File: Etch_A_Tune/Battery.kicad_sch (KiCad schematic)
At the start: 3 parts, among them IC1 BQ25170DSGR, U1 1042P, U2 BQ297xy

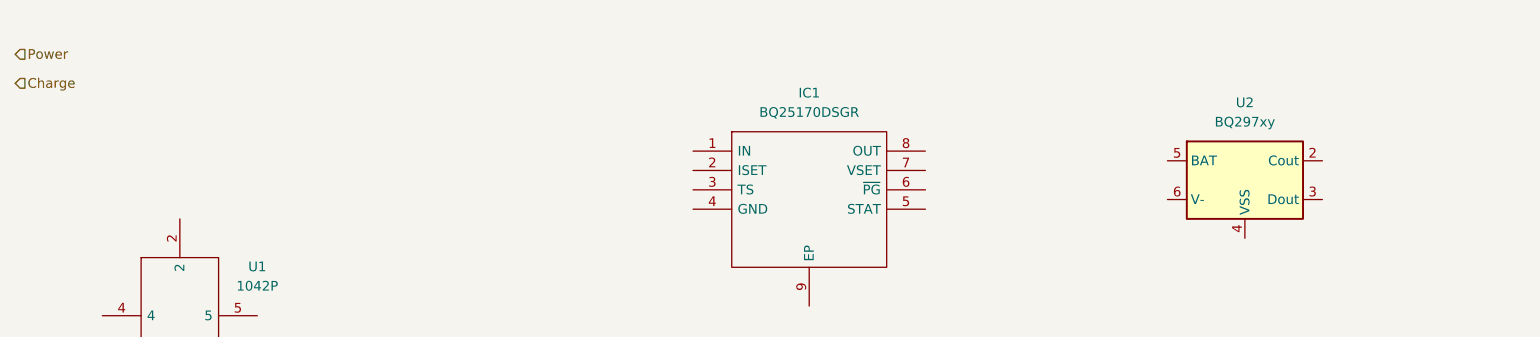
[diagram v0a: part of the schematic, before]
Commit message: Updated schematic and preliminary PCB doc
did rough PCB layout
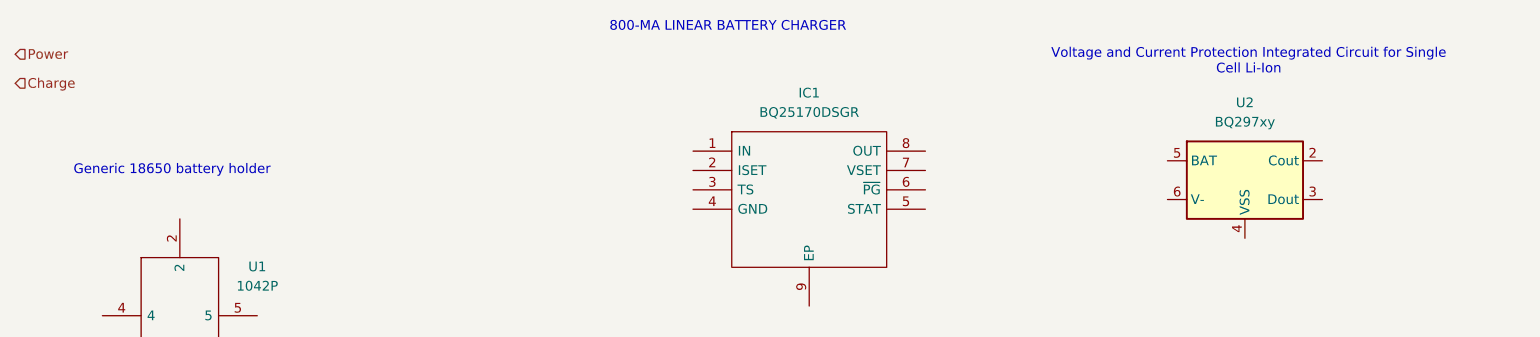
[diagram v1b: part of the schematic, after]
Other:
- note added: "800-MA LINEAR BATTERY CHARGER"
- note added: "Generic 18650 battery holder"
- note added: "Voltage and Current Protection Integrated Circuit for Single Cell Li-Ion"
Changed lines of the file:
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@@
 	(generator_version "9.0")
 	(paper "A4")
+	(text "800-MA LINEAR BATTERY CHARGER \n"
+		(exclude_from_sim no)
+		(at 140.462 45.974 0)
+		(effects
+			(font
+				(size 1.27 1.27)
+			)
+		)
+	)
+	(text "Generic 18650 battery holder\n"
+		(exclude_from_sim no)
+		(at 67.564 64.77 0)
+		(effects
+			(font
+				(size 1.27 1.27)
+			)
+		)
+	)
+	(text "Voltage and Current Protection Integrated Circuit for Single\nCell Li-Ion"
+		(exclude_from_sim no)
+		(at 208.788 50.546 0)
+		(effects
+			(font
+				(size 1.27 1.27)
+			)
+		)
+	)
 	(hierarchical_label "Charge"
 		(shape input)

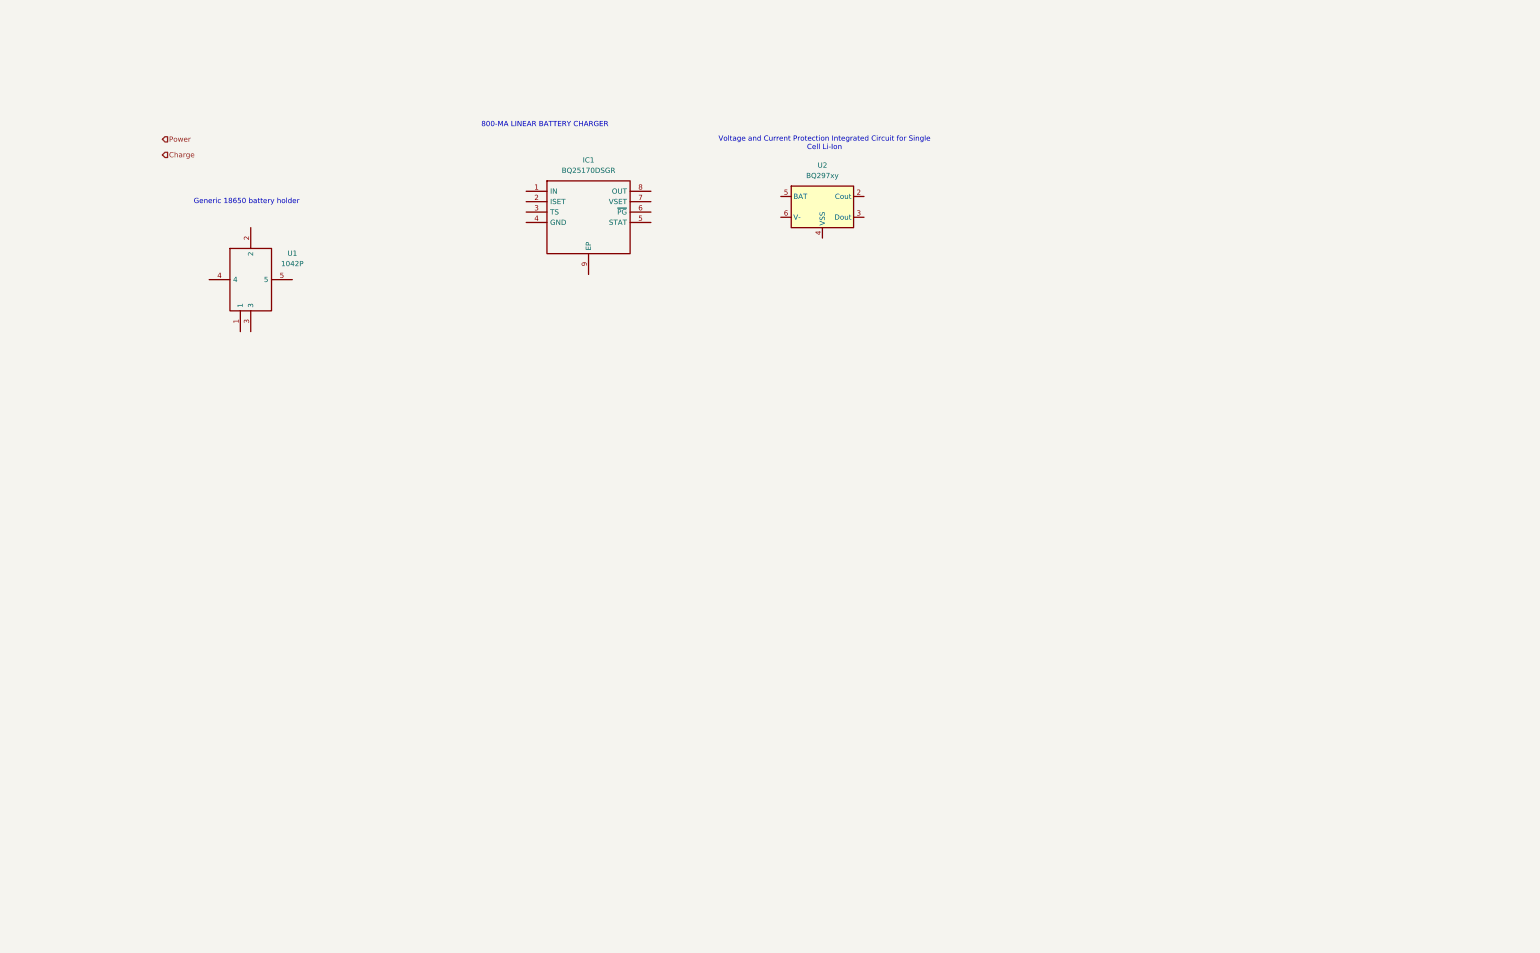
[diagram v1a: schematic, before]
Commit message: Schematic Update
Fixed component Footprints and added new switches/rotary encoders. Wired and placed bypass capacitors for most devices. Removed 5V boost converter because external DAC is no longer being utilized. Placed uC onto board design and implemented charging through USB-C connector.
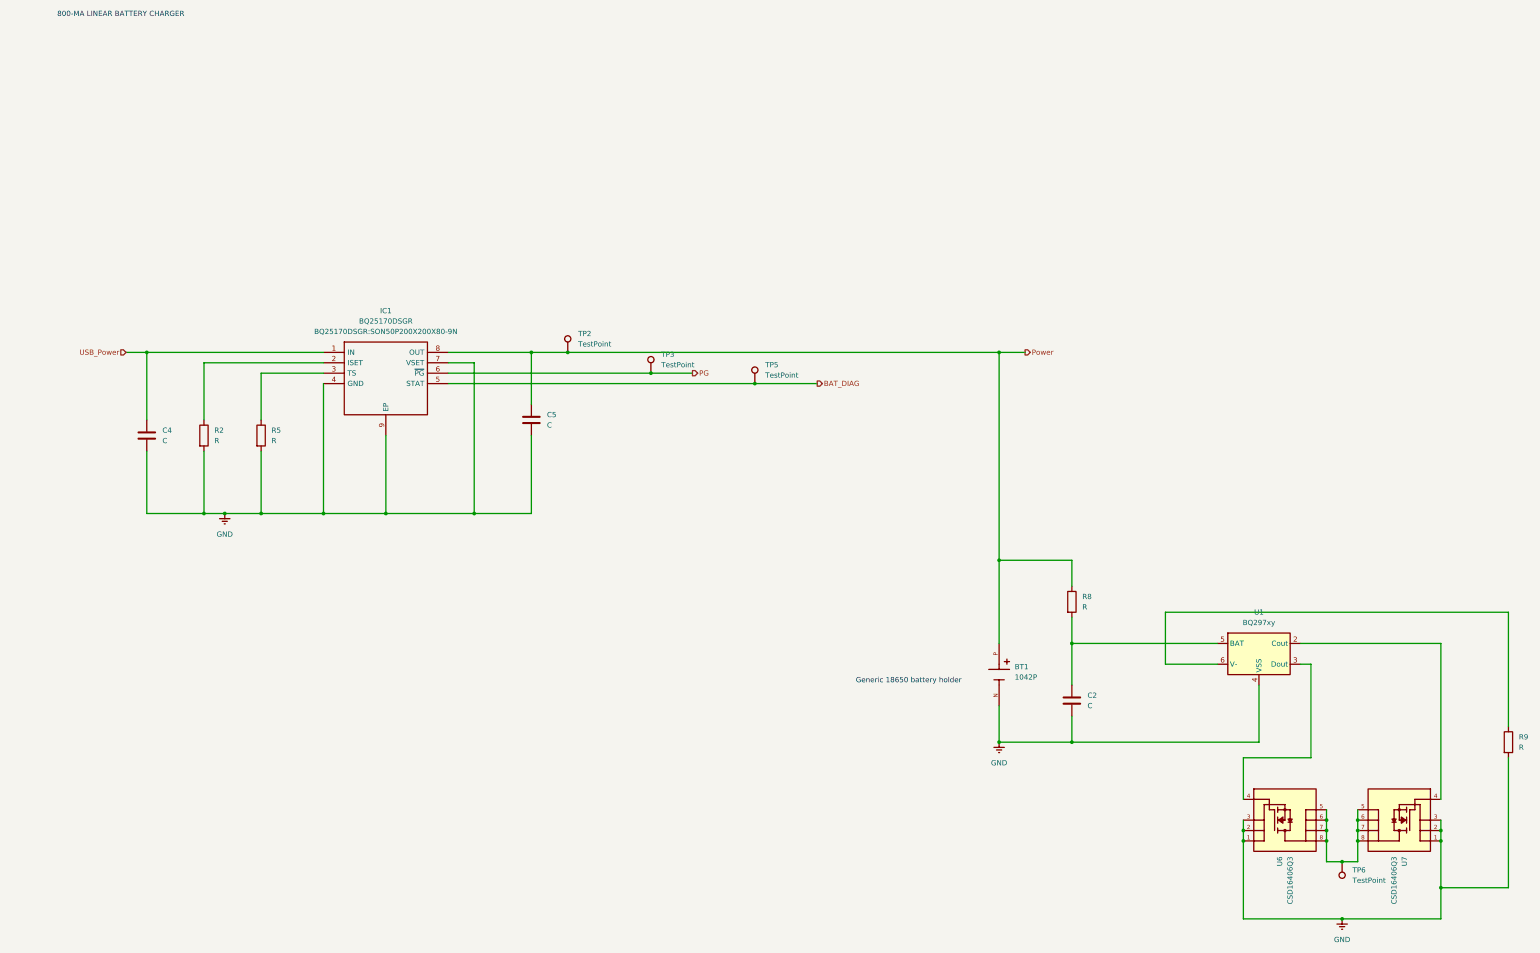
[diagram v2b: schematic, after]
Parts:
- removed U1: 1042P, 1042P, symbol SamacSys_Parts:1042P
- added BT1: 1042P, BQ25170DSGR:BAT_1042P, symbol 1042P:1042P
- added C2, C4, C5: C, symbol Device:C
- added R2, R5, R8, R9: R, symbol Device:R
- added TP2, TP3, TP5, TP6: TestPoint, TestPoint:TestPoint_Pad_D1.0mm, symbol Connector:TestPoint
- added U6, U7: CSD16406Q3, BQ25170DSGR:TRANS_CSD16406Q3, symbol CSD16406Q3:CSD16406Q3
- IC1: footprint SON50P200X200X80-9N -> BQ25170DSGR:SON50P200X200X80-9N
- renumbered U2 to U1
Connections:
- net Power: now also IC1.8 (OUT), BT1.P, C5.1, R8.1, TP2.1
- net USB_Power: now reaches IC1.1 (IN)
- net USB_Power: now also C4.1
- net at IC1.2 (ISET): now also R2.1
- net at IC1.3 (TS): now also R5.1
- net GND: now reaches IC1.4 (GND)
- net GND: now also IC1.7 (VSET), IC1.9 (EP), U1.4 (VSS), BT1.N, C2.2, C4.2, C5.2, R2.2, R5.2, R9.2, U6.1, U6.2, U6.3, U7.1, U7.2, U7.3
- net BAT_DIAG: now reaches IC1.5 (STAT)
- net BAT_DIAG: now also TP5.1
- net PG: now reaches IC1.6 (~{PG})
- net PG: now also TP3.1
- net at U1.2 (Cout): now also U7.4
- net at U1.3 (Dout): now also U6.4
- net at U1.5 (BAT): now also C2.1, R8.2
- net at U1.6 (V-): now also R9.1
- new net: TP6.1, U6.5, U6.6, U6.7, U6.8, U7.5, U7.6, U7.7, U7.8
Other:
- note removed: "Voltage and Current Protection Integrated Circuit for Single Cell Li-Ion"
- title: (none) -> Voltage and Current Protection Integrated Circuit for Single
- moved on the sheet: U1

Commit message: Etch A Tune V.02
Updated more foot prints and components onto bom, specifically SWD debug header and 1x14 pin header for touch and screen module. Added 4pin header for SD card reader.
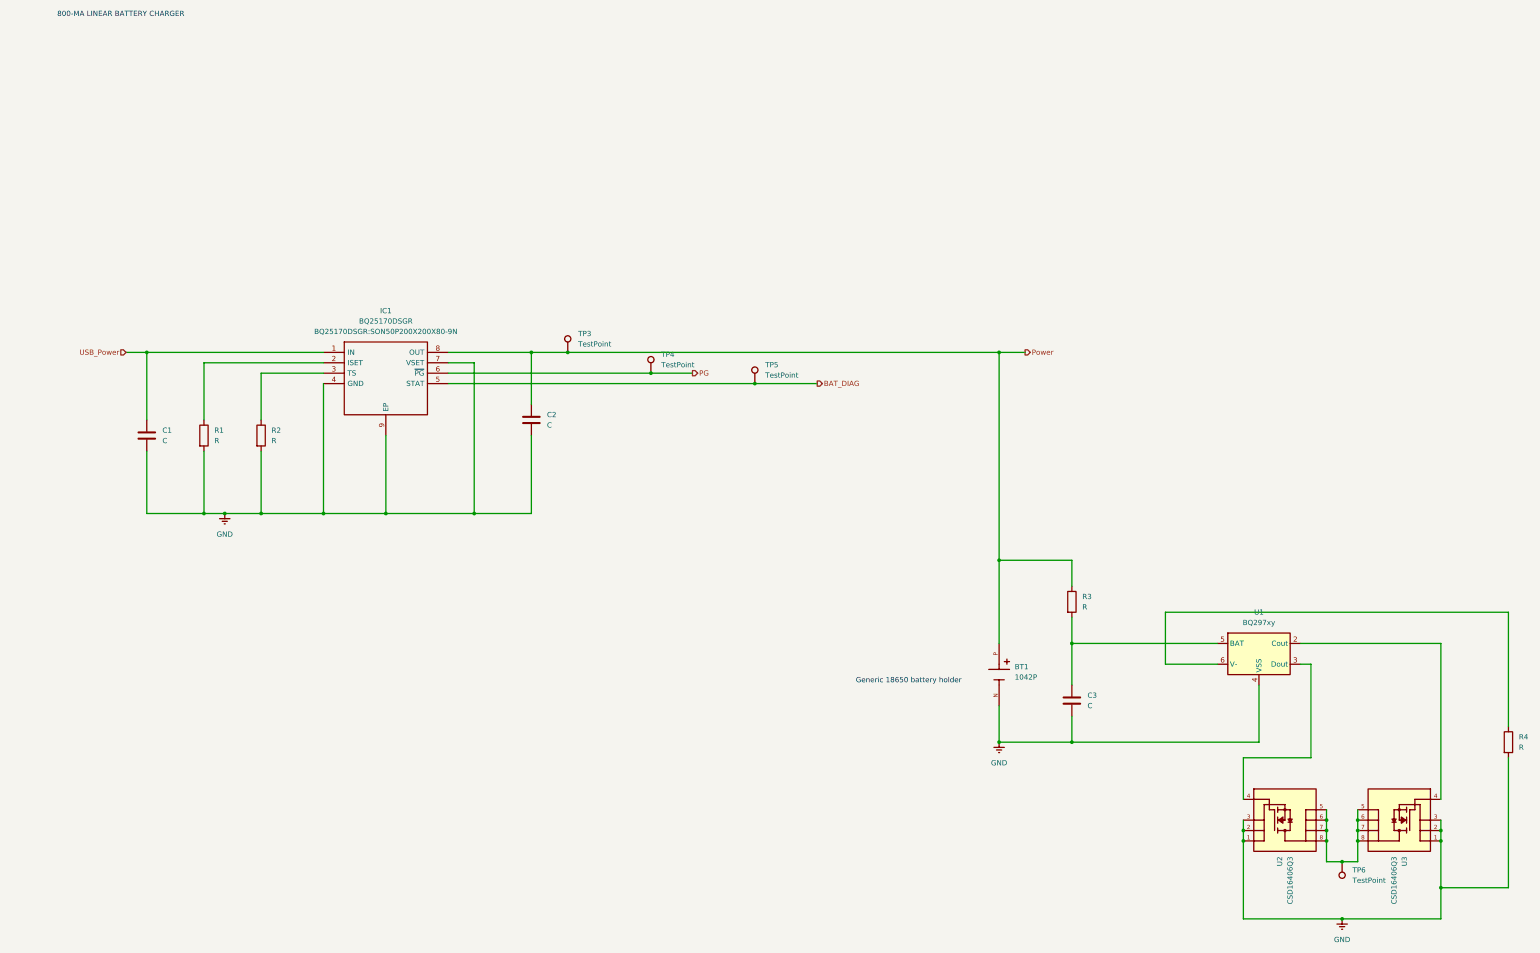
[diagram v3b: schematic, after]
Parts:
- renumbered C4 to C1, C5 to C2, C2 to C3, R2 to R1, R5 to R2, R8 to R3, R9 to R4, TP2 to TP3, TP3 to TP4, U6 to U2, U7 to U3
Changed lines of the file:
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@@
 		(on_board yes)
 		(dnp no)
-		(property "Reference" "U6"
+		(property "Reference" "U2"
 			(at 320.0399 224.79 90)
 			(effects
@@
 			(project ""
 				(path "/b4cdadf2-c4fe-48fe-ba6a-e15d1cad03b2/dd28cf9e-f503-4fc4-9cf8-d81b8295f9d5"
-					(reference "U6")
+					(reference "U2")
 					(unit 1)
 				)
@@
 		(dnp no)
 		(fields_autoplaced yes)
-		(property "Reference" "#PWR012"
+		(property "Reference" "#PWR05"
 			(at 62.23 147.32 0)
 			(effects
@@
 			(project "Etch_A_Tune"
 				(path "/b4cdadf2-c4fe-48fe-ba6a-e15d1cad03b2/dd28cf9e-f503-4fc4-9cf8-d81b8295f9d5"
-					(reference "#PWR012")
+					(reference "#PWR05")
 					(unit 1)
 				)
@@
 		(on_board yes)
 		(dnp no)
-		(property "Reference" "U7"
+		(property "Reference" "U3"
 			(at 350.5201 224.79 90)
 			(effects
@@
 			(project "Etch_A_Tune"
 				(path "/b4cdadf2-c4fe-48fe-ba6a-e15d1cad03b2/dd28cf9e-f503-4fc4-9cf8-d81b8295f9d5"
-					(reference "U7")
+					(reference "U3")
 					(unit 1)
 				)
@@
 		(dnp no)
 		(fields_autoplaced yes)
-		(property "Reference" "C2"
+		(property "Reference" "C3"
 			(at 273.05 185.4199 0)
 			(effects
@@
 			(project "Etch_A_Tune"
 				(path "/b4cdadf2-c4fe-48fe-ba6a-e15d1cad03b2/dd28cf9e-f503-4fc4-9cf8-d81b8295f9d5"
-					(reference "C2")
+					(reference "C3")
 					(unit 1)
 				)
@@
 		(dnp no)
 		(fields_autoplaced yes)
-		(property "Reference" "R2"
+		(property "Reference" "R1"
 			(at 59.69 120.6499 0)
 			(effects
@@
 			(project "Etch_A_Tune"
 				(path "/b4cdadf2-c4fe-48fe-ba6a-e15d1cad03b2/dd28cf9e-f503-4fc4-9cf8-d81b8295f9d5"
-					(reference "R2")
+					(reference "R1")
 					(unit 1)
 				)
@@
 		(dnp no)
 		(fields_autoplaced yes)
-		(property "Reference" "R5"
+		(property "Reference" "R2"
 			(at 73.66 120.6499 0)
 			(effects
@@
 			(project "Etch_A_Tune"
 				(path "/b4cdadf2-c4fe-48fe-ba6a-e15d1cad03b2/dd28cf9e-f503-4fc4-9cf8-d81b8295f9d5"
-					(reference "R5")
+					(reference "R2")
 					(unit 1)
 				)
@@
 		(dnp no)
 		(fields_autoplaced yes)
-		(property "Reference" "C4"
+		(property "Reference" "C1"
 			(at 46.99 120.6499 0)
 			(effects
@@
 			(project "Etch_A_Tune"
 				(path "/b4cdadf2-c4fe-48fe-ba6a-e15d1cad03b2/dd28cf9e-f503-4fc4-9cf8-d81b8295f9d5"
-					(reference "C4")
+					(reference "C1")
 					(unit 1)
 				)
@@
 		(dnp no)
 		(fields_autoplaced yes)
-		(property "Reference" "TP3"
+		(property "Reference" "TP4"
 			(at 168.91 102.1079 0)
 			(effects
@@
 			(project "Etch_A_Tune"
 				(path "/b4cdadf2-c4fe-48fe-ba6a-e15d1cad03b2/dd28cf9e-f503-4fc4-9cf8-d81b8295f9d5"
-					(reference "TP3")
+					(reference "TP4")
 					(unit 1)
 				)
@@
 		(dnp no)
 		(fields_autoplaced yes)
-		(property "Reference" "#PWR011"
+		(property "Reference" "#PWR07"
 			(at 335.28 246.38 0)
 			(effects
@@
 			(project "Etch_A_Tune"
 				(path "/b4cdadf2-c4fe-48fe-ba6a-e15d1cad03b2/dd28cf9e-f503-4fc4-9cf8-d81b8295f9d5"
-					(reference "#PWR011")
+					(reference "#PWR07")
 					(unit 1)
 				)
@@
 		(dnp no)
 		(fields_autoplaced yes)
-		(property "Reference" "R9"
+		(property "Reference" "R4"
 			(at 378.46 195.5799 0)
 			(effects
@@
 			(project "Etch_A_Tune"
 				(path "/b4cdadf2-c4fe-48fe-ba6a-e15d1cad03b2/dd28cf9e-f503-4fc4-9cf8-d81b8295f9d5"
-					(reference "R9")
+					(reference "R4")
 					(unit 1)
 				)
@@
 		(dnp no)
 		(fields_autoplaced yes)
-		(property "Reference" "TP2"
+		(property "Reference" "TP3"
 			(at 148.59 97.0279 0)
 			(effects
@@
 			(project "Etch_A_Tune"
 				(path "/b4cdadf2-c4fe-48fe-ba6a-e15d1cad03b2/dd28cf9e-f503-4fc4-9cf8-d81b8295f9d5"
-					(reference "TP2")
+					(reference "TP3")
 					(unit 1)
 				)
@@
 		(dnp no)
 		(fields_autoplaced yes)
-		(property "Reference" "R8"
+		(property "Reference" "R3"
 			(at 271.78 161.2899 0)
 			(effects
@@
 			(project "Etch_A_Tune"
 				(path "/b4cdadf2-c4fe-48fe-ba6a-e15d1cad03b2/dd28cf9e-f503-4fc4-9cf8-d81b8295f9d5"
-					(reference "R8")
+					(reference "R3")
 					(unit 1)
 				)
@@
 		(dnp no)
 		(fields_autoplaced yes)
-		(property "Reference" "C5"
+		(property "Reference" "C2"
 			(at 140.97 116.8399 0)
 			(effects
@@
 			(project "Etch_A_Tune"
 				(path "/b4cdadf2-c4fe-48fe-ba6a-e15d1cad03b2/dd28cf9e-f503-4fc4-9cf8-d81b8295f9d5"
-					(reference "C5")
+					(reference "C2")
 					(unit 1)
 				)
@@
 		(dnp no)
 		(fields_autoplaced yes)
-		(property "Reference" "#PWR02"
+		(property "Reference" "#PWR06"
 			(at 251.46 203.2 0)
 			(effects
@@
 			(project "Etch_A_Tune"
 				(path "/b4cdadf2-c4fe-48fe-ba6a-e15d1cad03b2/dd28cf9e-f503-4fc4-9cf8-d81b8295f9d5"
-					(reference "#PWR02")
-					(unit 1)
-				)
+					(reference "#PWR06")
+					(unit 1)
+				)

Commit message: Updated parallel power supply
Updated USB and battery operation and added DAC output
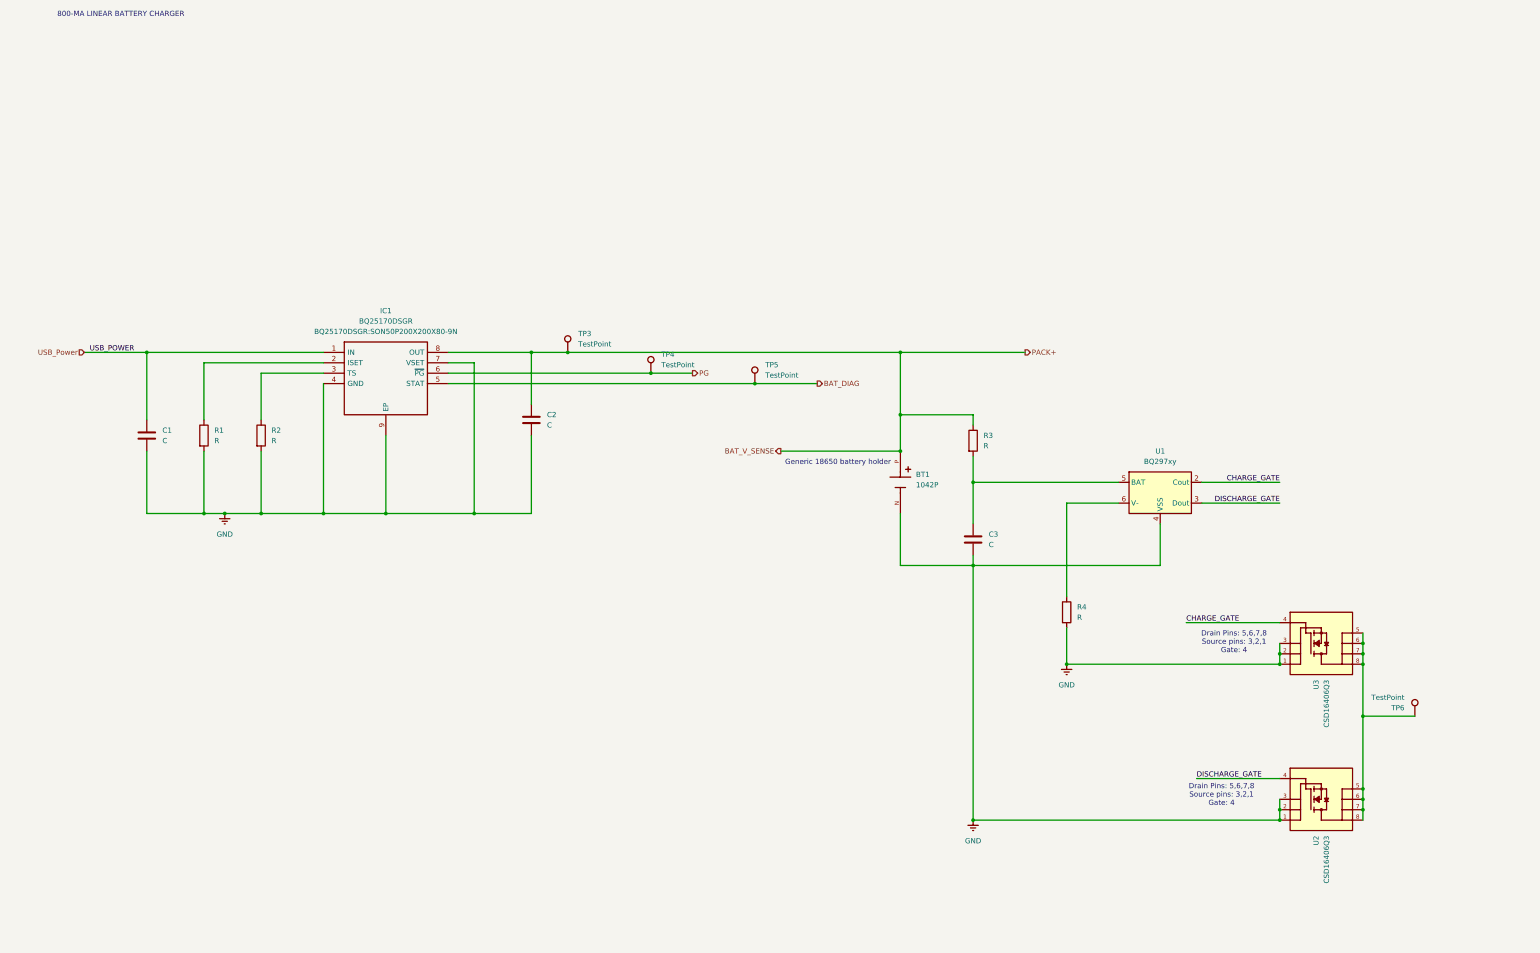
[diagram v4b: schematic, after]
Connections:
- net DISCHARGE_GATE: now reaches U1.3 (Dout), U2.4
- net CHARGE_GATE: now reaches U1.2 (Cout), U3.4
- net Power renamed BAT_V_SENSE
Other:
- note added: "Drain Pins: 5,6,7,8 Source pins: 3,2,1 Gate: 4"
- moved on the sheet: BT1, C3, R3, R4, TP6, U1, U2, U3
